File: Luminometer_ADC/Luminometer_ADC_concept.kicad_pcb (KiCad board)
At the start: 4 copper layers, 65 x 50 mm, 57 parts, among them J1 Harting__15210122401000, U1 LT3464, U2 ADA4522-1, U3 ADR512, U4 ADR512, U5 ADA4522-4, U6 LP5907MFX-3, U7 ADS131M08IPBS

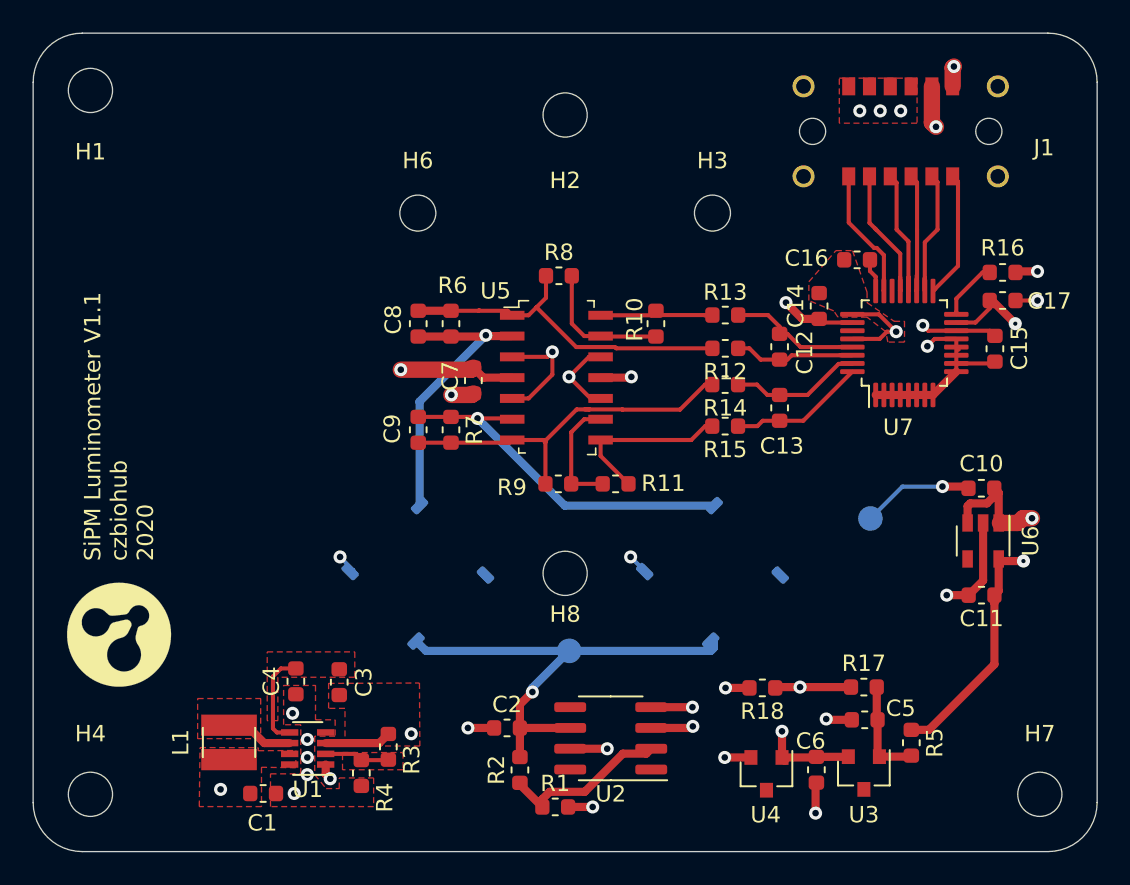
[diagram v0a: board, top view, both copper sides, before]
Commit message: Submitted for fab: V1.1 ADC board
RPi board dev:
- Move RPi headers to bottom of PCB for better mechanical fit
- Co-optimize mechanical layout w/ solid model
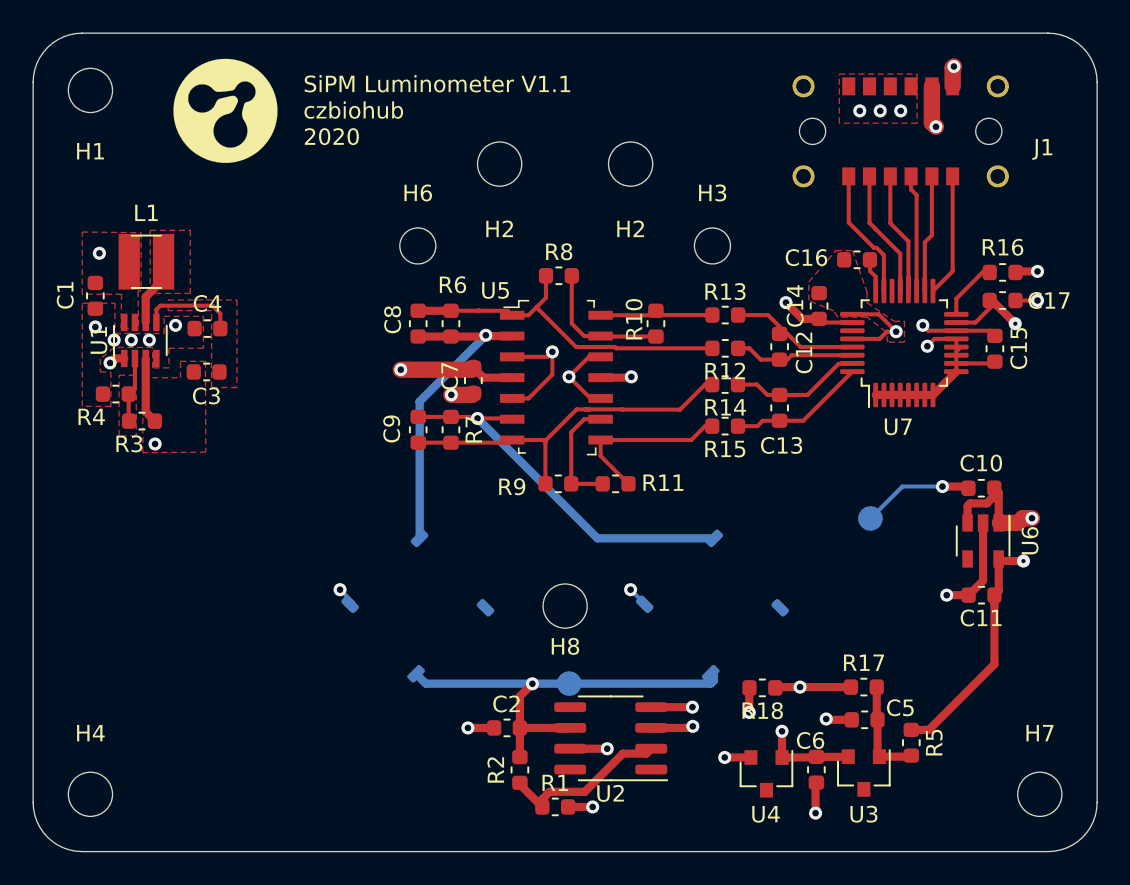
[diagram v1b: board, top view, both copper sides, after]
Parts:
- added H2: MountingHole, MountingHole:MountingHole_2.7mm_M2.5, F.Cu at (151.5, 88.0)
- moved G*** 32.7 mm to (126.8, 84.8)
- moved C1 32.1 mm to (118.8, 96.0), turned to 270 degrees
- moved L1 29.8 mm to (121.9, 94.0), turned to 0 degrees
- moved R4 27.6 mm to (120.0, 102.0), turned to 180 degrees
- moved U1 26.9 mm to (121.5, 98.8), turned to 90 degrees
- moved R3 25.0 mm to (121.7, 103.7), turned to 180 degrees
- moved C4 22.2 mm to (125.7, 98.0), turned to 180 degrees
- moved C3 20.6 mm to (125.6, 100.7), turned to 0 degrees
- moved G*** 12.8 mm to (124.5, 112.0)
- moved H2 5.00 mm to (143.5, 88.0)
- moved H3 2.01 mm to (156.5, 93.0)
- moved H6 2.01 mm to (138.5, 93.0)
- moved Bias 2.00 mm to (147.8, 119.7)
- moved H8 2.00 mm to (147.5, 115.0)
- moved SiPM1 2.00 mm to (138.5, 115.0)
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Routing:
- net +34V: track 18.8 -> 41.8 mm
- net +5V: track 129.9 -> 136.2 mm
- net /BIAS: track 29.9 -> 27.0 mm
- net Net-(C8-Pad2): track 18.4 -> 20.4 mm
- net /SCLK: track 8.19 -> 7.25 mm
- net Net-(C9-Pad1): track 22.9 -> 23.7 mm
